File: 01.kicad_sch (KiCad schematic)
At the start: 1 part

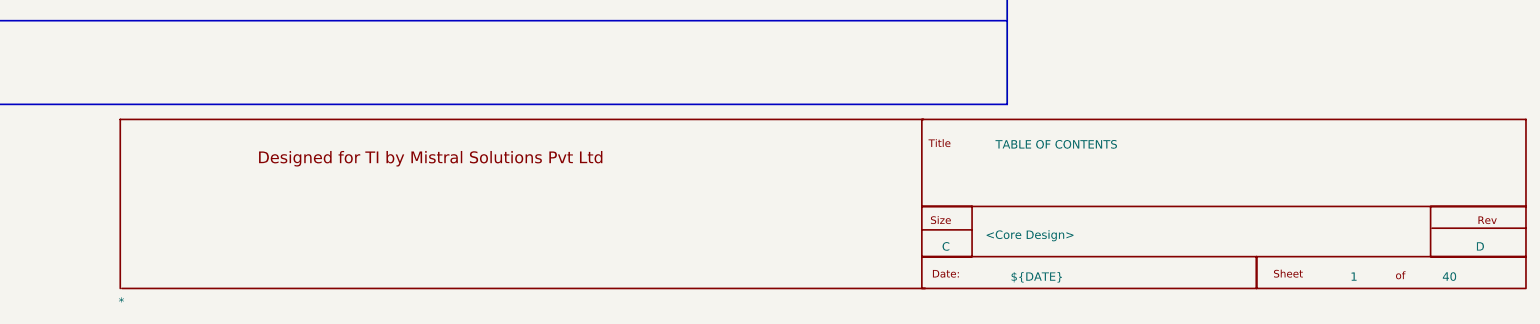
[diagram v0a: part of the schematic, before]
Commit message: fix joint, offpage, and typo
DRC errors are cleared, some warnings remain.
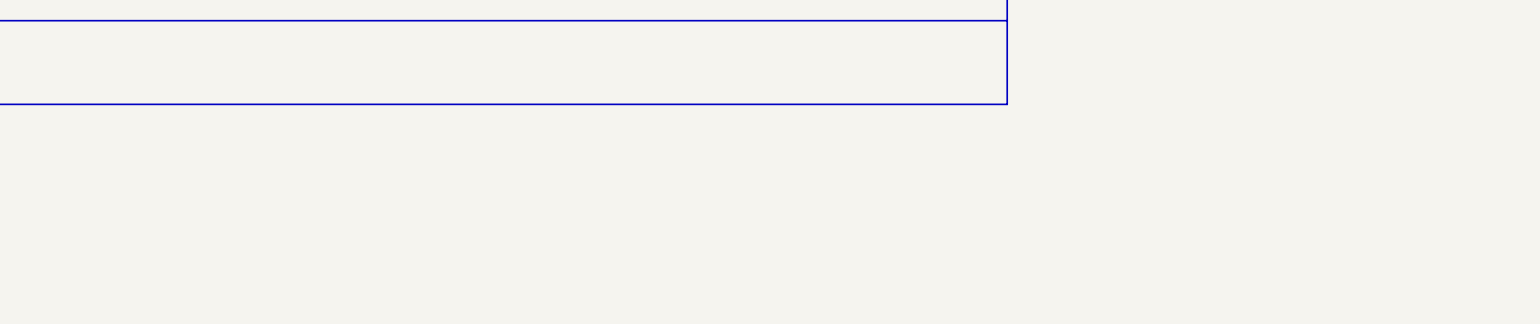
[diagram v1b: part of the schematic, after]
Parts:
- removed *: MISTRAL_TITLEBLK_CSIZE, symbol 01-altium-import:root_0_MISTRAL_TITLEBLK_CSIZE
